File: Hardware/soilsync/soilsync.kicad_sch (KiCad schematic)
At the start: 3 parts, among them J1 Barrel_Jack_Switch, U1 STM32F103C8Tx, U2 LM2596

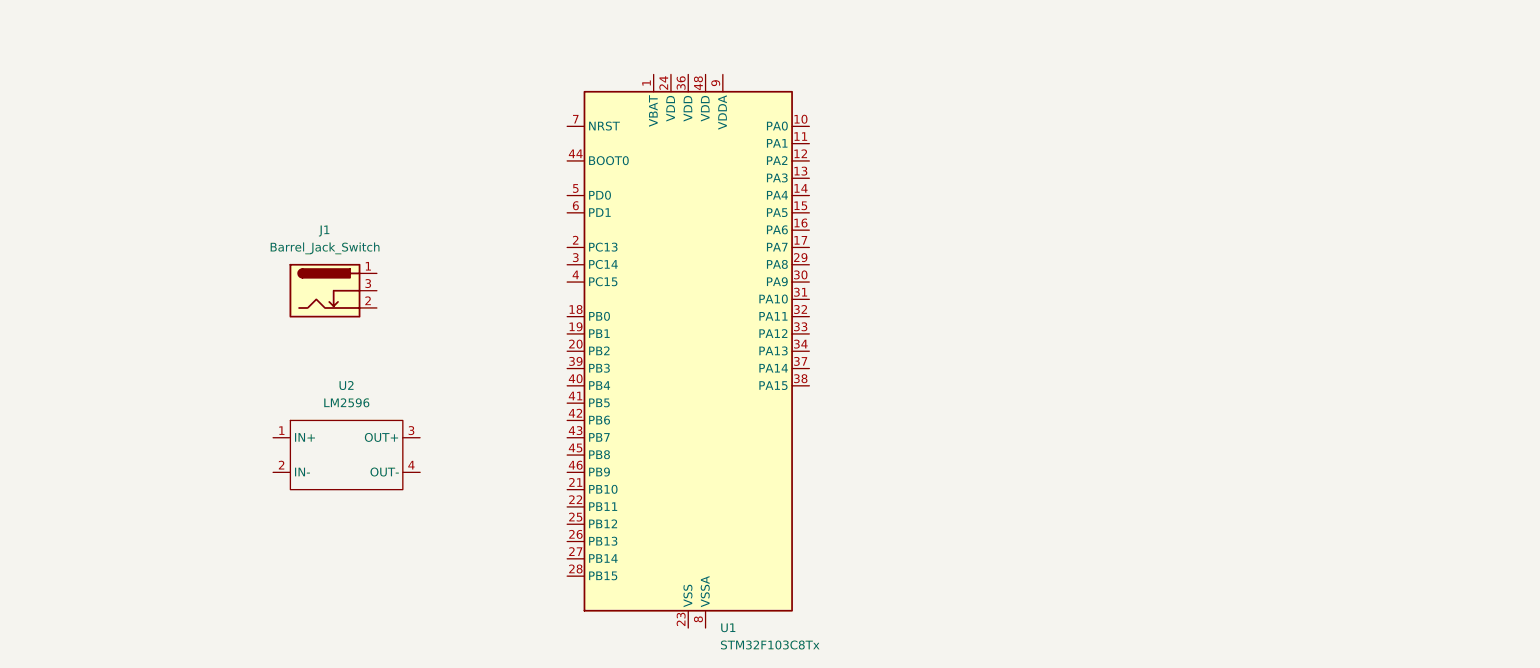
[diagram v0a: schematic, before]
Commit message: summary after classes
failed to create 3D model
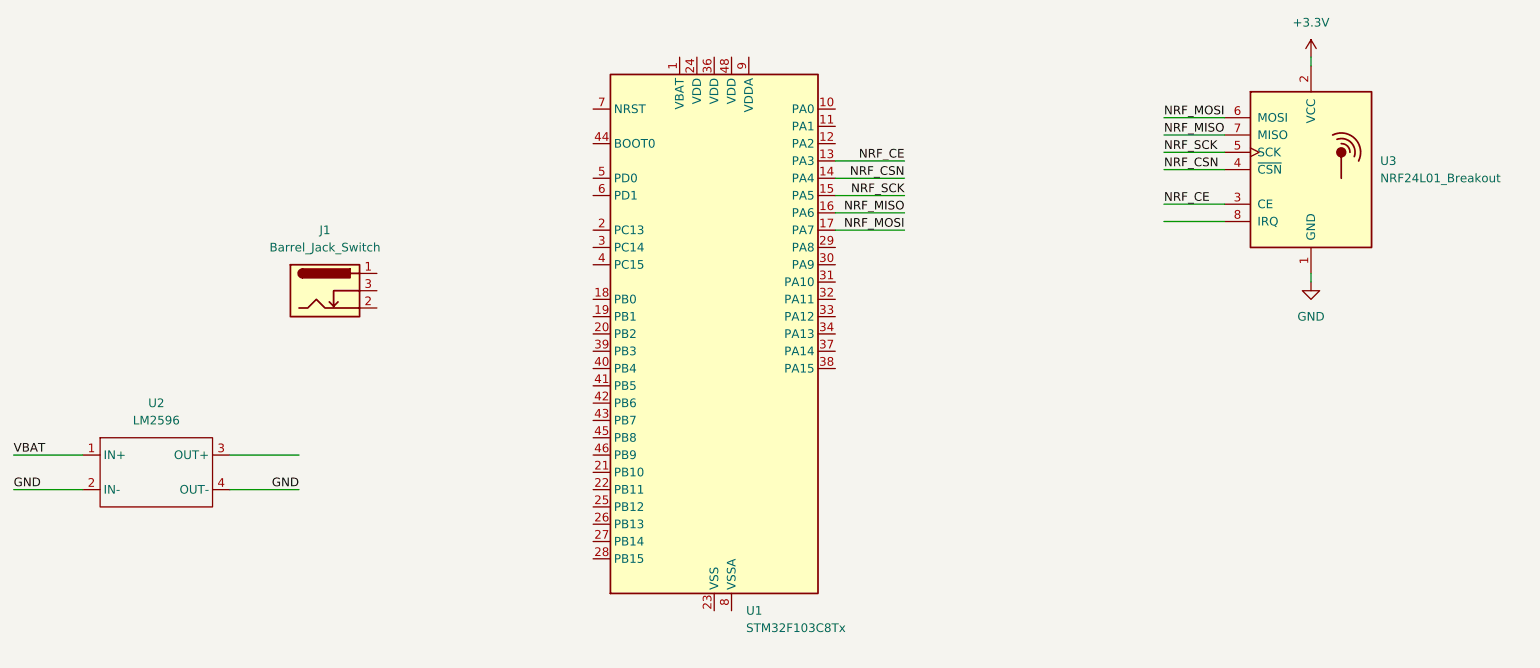
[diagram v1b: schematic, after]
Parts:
- added U3: NRF24L01_Breakout, RF_Module:nRF24L01_Breakout, symbol RF:NRF24L01_Breakout
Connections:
- net VBAT: now reaches U2.1 (IN+)
- net GND: now reaches U2.2 (IN-)
- net GND: now also U2.4 (OUT-), U3.1 (GND)
- net NRF_CE: now reaches U1.13 (PA3)
- net NRF_CE: now also U3.3 (CE)
- net NRF_CSN: now reaches U1.14 (PA4)
- net NRF_CSN: now also U3.4 (~{CSN})
- net NRF_SCK: now reaches U1.15 (PA5)
- net NRF_SCK: now also U3.5 (SCK)
- net NRF_MISO: now reaches U1.16 (PA6)
- net NRF_MISO: now also U3.7 (MISO)
- net NRF_MOSI: now reaches U1.17 (PA7)
- net NRF_MOSI: now also U3.6 (MOSI)
- new net +3.3V: U3.2 (VCC)
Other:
- moved on the sheet: U1, U2

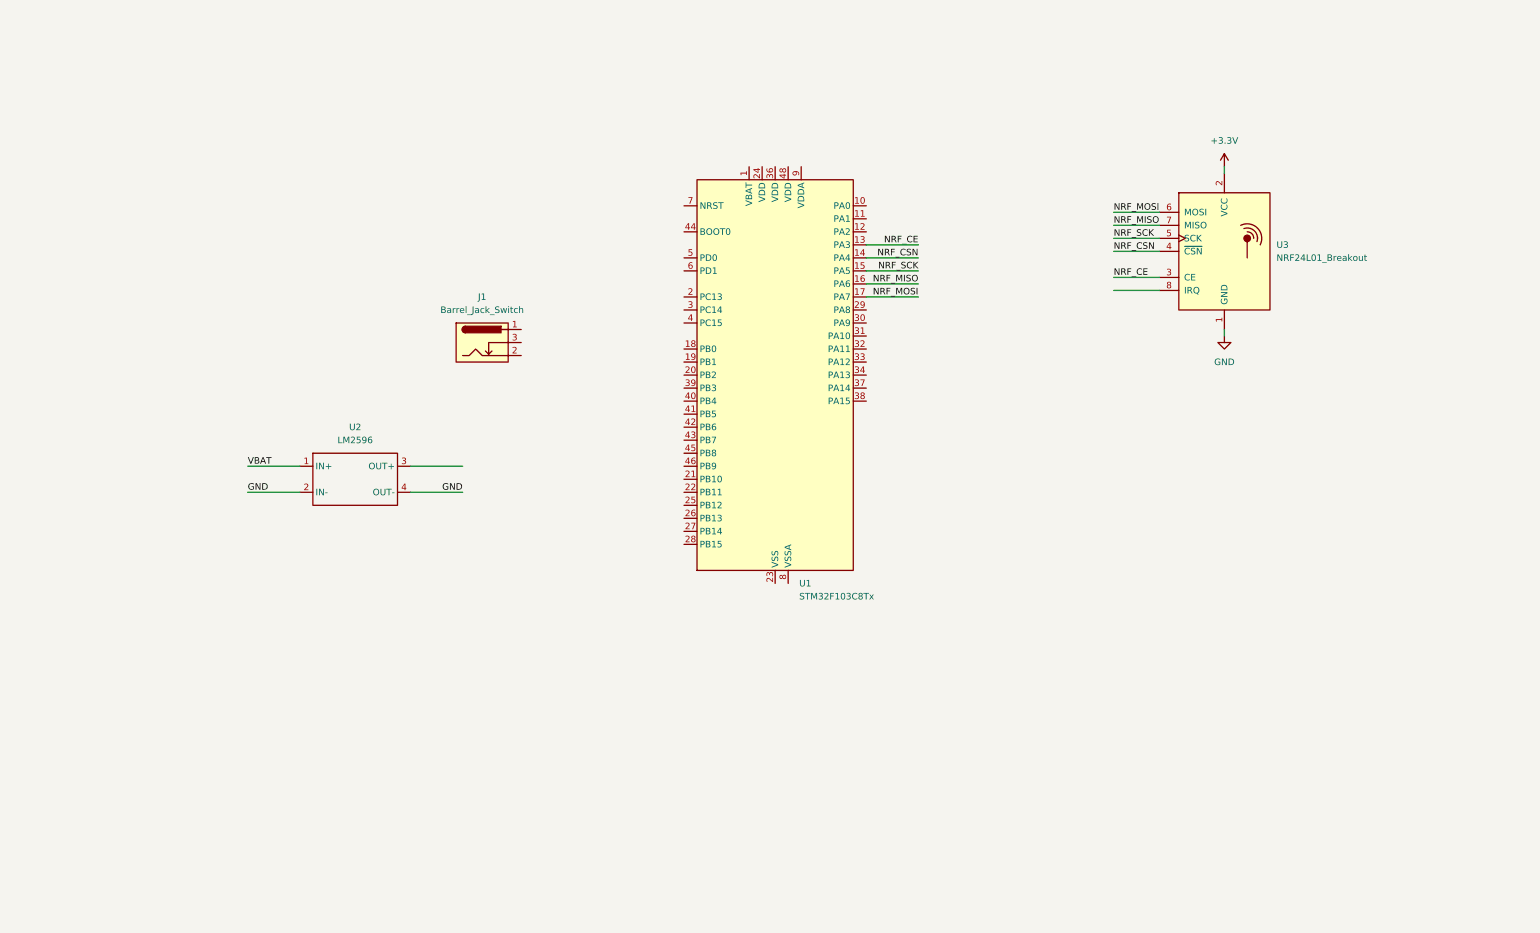
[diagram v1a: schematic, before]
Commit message: updated in kicad
added custom components
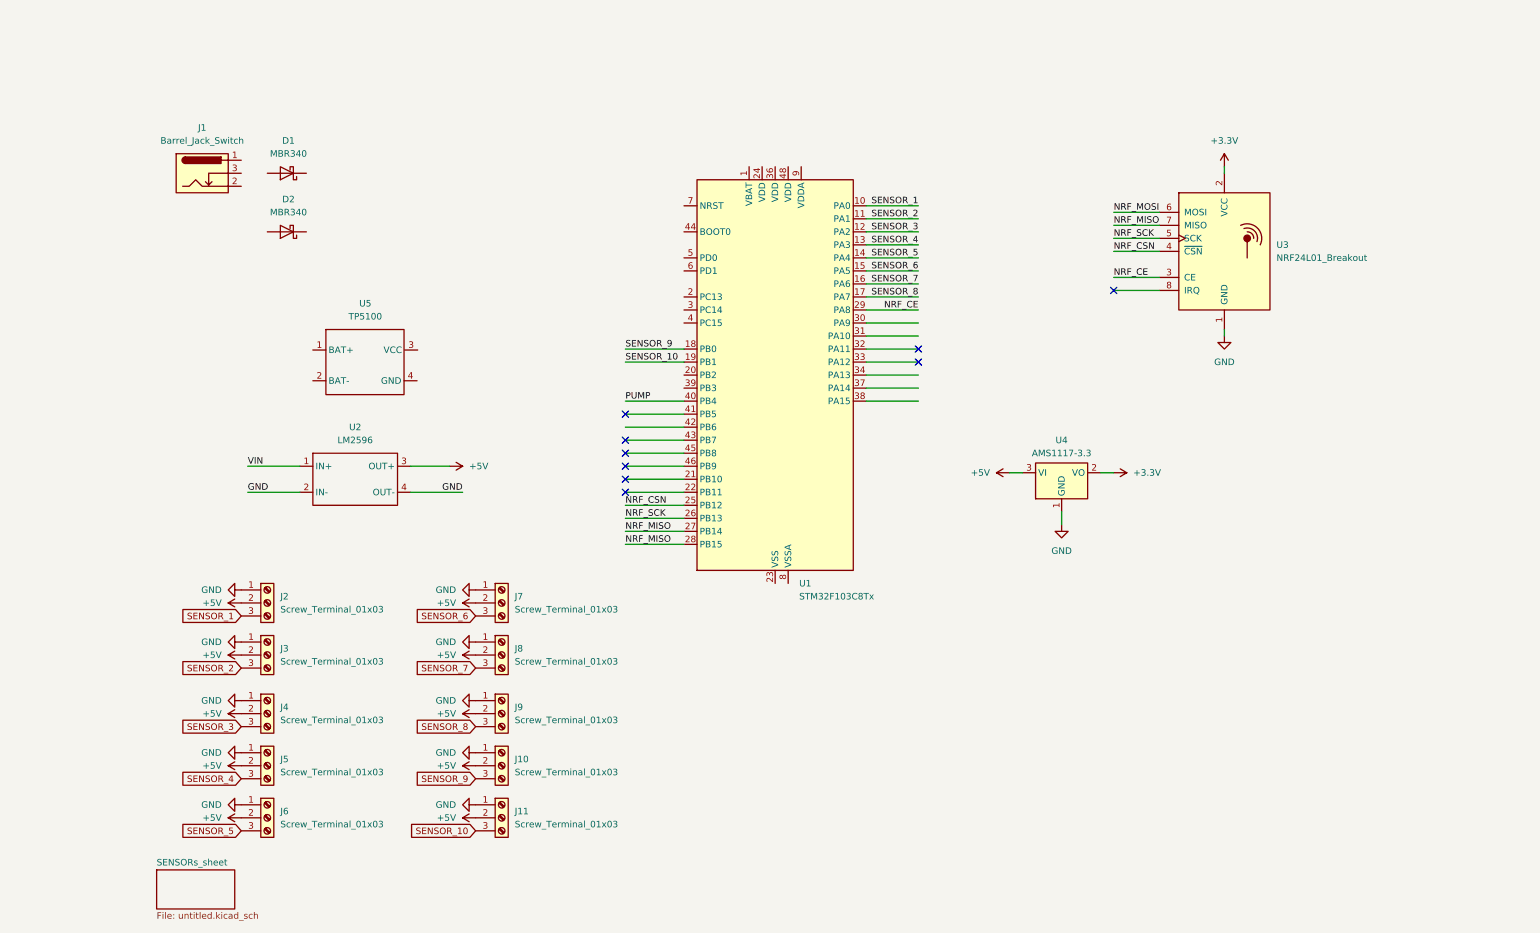
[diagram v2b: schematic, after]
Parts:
- added D1, D2: MBR340, Diode_THT:D_DO-201AD_P15.24mm_Horizontal, symbol Diode:MBR340
- added J10, J11, J2, J3, J4, J5, J6, J7, J8, J9: Screw_Terminal_01x03, TerminalBlock_4Ucon:TerminalBlock_4Ucon_1x03_P3.50mm_Horizontal, symbol Connector:Screw_Terminal_01x03
- added U4: AMS1117-3.3, Package_TO_SOT_SMD:SOT-223-3_TabPin2, symbol Regulator_Linear:AMS1117-3.3
- added U5: TP5100, Modules:TP5100_Module, symbol TP5100:TP5100_Module
- J1: footprint (none) -> Connector_BarrelJack:BarrelJack_Horizontal
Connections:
- net +3.3V: now also U4.2 (VO)
- net GND: now also J10.1 (Pin_1), J11.1 (Pin_1), J2.1 (Pin_1), J3.1 (Pin_1), J4.1 (Pin_1), J5.1 (Pin_1), J6.1 (Pin_1), J7.1 (Pin_1), J8.1 (Pin_1), J9.1 (Pin_1), U4.1 (GND)
- net NRF_CE: now also U1.29 (PA8); no longer U1.13 (PA3)
- net NRF_CSN: now also U1.25 (PB12); no longer U1.14 (PA4)
- net NRF_MISO: now also U1.27 (PB14), U1.28 (PB15); no longer U1.16 (PA6)
- net NRF_MOSI: no longer U1.17 (PA7)
- net NRF_SCK: now also U1.26 (PB13); no longer U1.15 (PA5)
- net +5V: now reaches U2.3 (OUT+)
- net +5V: now also J10.2 (Pin_2), J11.2 (Pin_2), J2.2 (Pin_2), J3.2 (Pin_2), J4.2 (Pin_2), J5.2 (Pin_2), J6.2 (Pin_2), J7.2 (Pin_2), J8.2 (Pin_2), J9.2 (Pin_2), U4.3 (VI)
- net SENSOR_1: now reaches U1.10 (PA0)
- net SENSOR_1: now also J2.3 (Pin_3)
- net SENSOR_2: now reaches U1.11 (PA1)
- net SENSOR_2: now also J3.3 (Pin_3)
- net SENSOR_3: now reaches U1.12 (PA2)
- net SENSOR_3: now also J4.3 (Pin_3)
- net SENSOR_9: now reaches U1.18 (PB0)
- net SENSOR_9: now also J10.3 (Pin_3)
- net SENSOR_10: now reaches U1.19 (PB1)
- net SENSOR_10: now also J11.3 (Pin_3)
- net PUMP: now reaches U1.40 (PB4)
- net VBAT renamed VIN
- new net SENSOR_4: J5.3 (Pin_3), U1.13 (PA3)
- new net SENSOR_5: J6.3 (Pin_3), U1.14 (PA4)
- new net SENSOR_6: J7.3 (Pin_3), U1.15 (PA5)
- new net SENSOR_7: J8.3 (Pin_3), U1.16 (PA6)
- new net SENSOR_8: J9.3 (Pin_3), U1.17 (PA7)
- no-connect marks 0 -> 9
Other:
- added sheet SENSORs_sheet (untitled.kicad_sch)
- moved on the sheet: J1

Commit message: a little changes in footprints
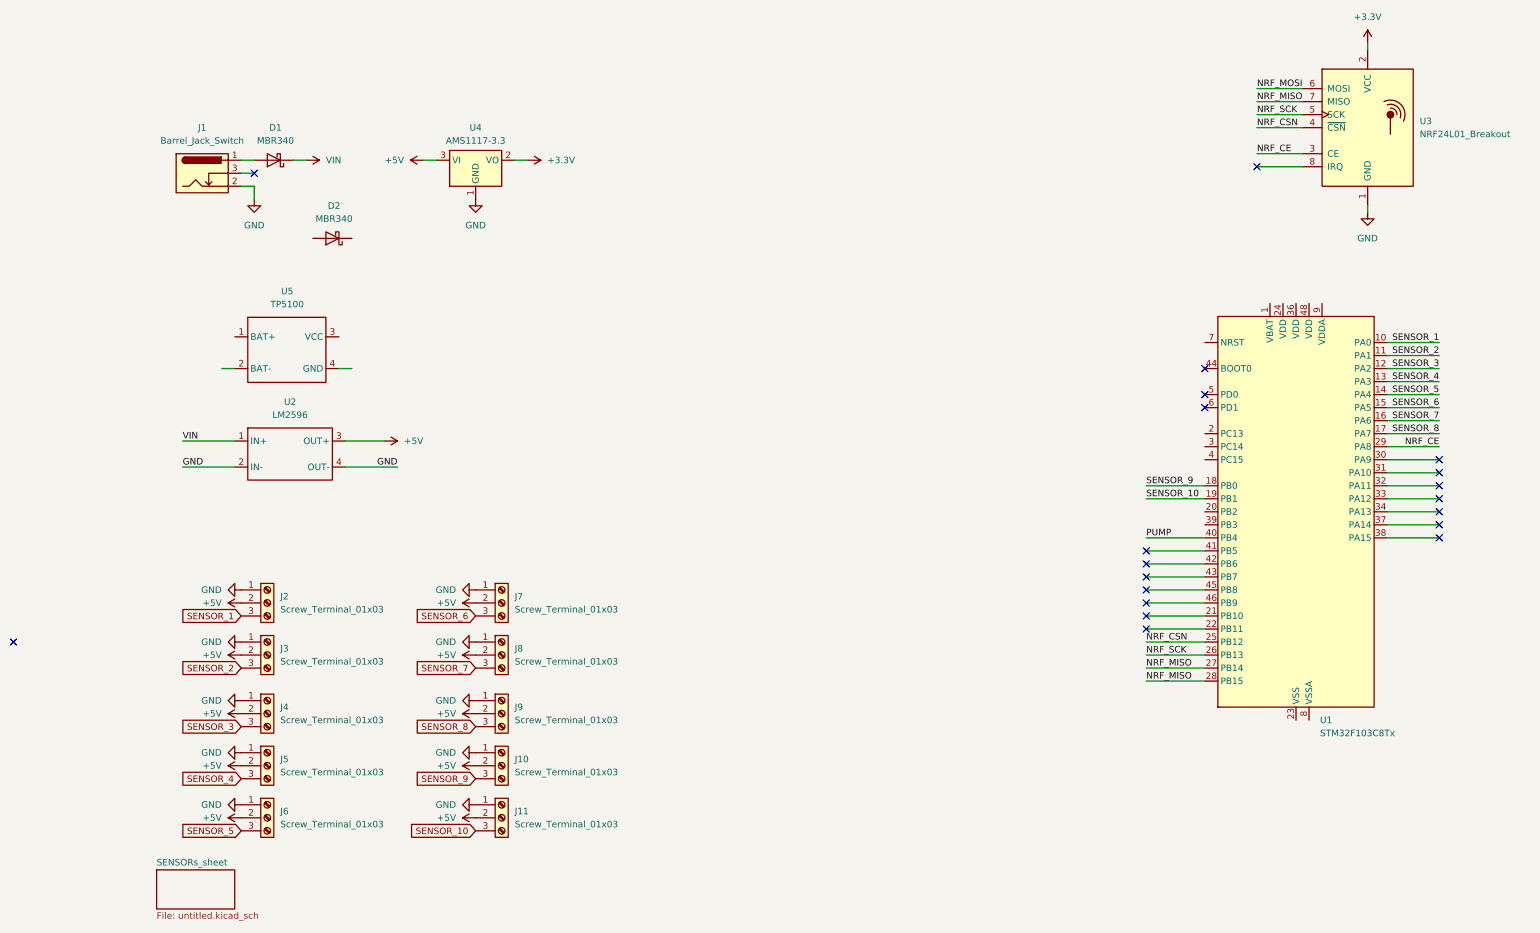
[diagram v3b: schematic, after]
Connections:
- net GND: now also J1.2
- net VIN: now also D1.1 (K)
- net at D1.2 (A): now also J1.1
- no-connect marks 9 -> 20
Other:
- moved on the sheet: D1, D2, U1, U2, U3, U4, U5

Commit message: custom components adjustments
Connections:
- net GND: now also U5.4 (GND)
- net VIN: now also U5.3 (VCC)
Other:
- removed sheet SENSORs_sheet
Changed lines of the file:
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@@
 	(wire
 		(pts
-			(xy 52.07 87.63) (xy 54.61 87.63)
+			(xy 52.07 87.63) (xy 57.15 87.63)
 		)
 		(stroke
@@
 	(wire
 		(pts
+			(xy 29.21 82.55) (xy 31.75 82.55)
+		)
+		(stroke
+			(width 0)
+			(type default)
+		)
+	)
+	(wire
+		(pts
 			(xy 53.34 101.76) (xy 60.96 101.76)
 		)
@@
 	(wire
 		(pts
+			(xy 57.15 87.63) (xy 57.15 88.9)
+		)
+		(stroke
+			(width 0)
+			(type default)
+		)
+	)
+	(wire
+		(pts
 			(xy 68.58 46.99) (xy 71.12 46.99)
 		)
@@
 	(wire
 		(pts
+			(xy 52.07 82.55) (xy 57.15 82.55)
+		)
+		(stroke
+			(width 0)
+			(type default)
+		)
+	)
+	(wire
+		(pts
 			(xy 33.02 46.99) (xy 35.56 46.99)
 		)
@@
 		)
 	)
+	(label "VIN"
+		(at 57.15 82.55 180)
+		(effects
+			(font
+				(size 1.27 1.27)
+			)
+			(justify right bottom)
+		)
+	)
 	(label "SENSOR_1"
 		(at 266.7 82.55 180)
@@
 	)
 	(symbol
-		(lib_id "power:+5V")
-		(at 78.74 154.94 90)
+		(lib_id "power:GND")
+		(at 57.15 88.9 0)
 		(unit 1)
 		(exclude_from_sim no)
@@
 		(dnp no)
 		(fields_autoplaced yes)
-		(property "Reference" "#PWR014"
-			(at 82.55 154.94 0)
+		(property "Reference" "#PWR029"
+			(at 57.15 95.25 0)
 			(effects
 				(font
@@
 			)
 		)
-		(property "Value" "+5V"
-			(at 74.93 154.9399 90)
+		(property "Value" "GND"
+			(at 57.15 93.98 0)
 			(effects
 				(font
 					(size 1.27 1.27)
 				)
-				(justify left)
 			)
 		)
 		(property "Footprint" ""
-			(at 78.74 154.94 0)
+			(at 57.15 88.9 0)
 			(effects
 				(font
@@
 		)
 		(property "Datasheet" ""
-			(at 78.74 154.94 0)
+			(at 57.15 88.9 0)
 			(effects
 				(font
@@
 			)
 		)
-		(property "Description" "Power symbol creates a global label with name \"+5V\""
-			(at 78.74 154.94 0)
+		(property "Description" "Power symbol creates a global label with name \"GND\" , ground"
+			(at 57.15 88.9 0)
 			(effects
 				(font
@@
 			(project ""
 				(path "/3e3c5228-e247-4567-a085-5b3516ef26ec"
-					(reference "#PWR014")
+					(reference "#PWR029")
 					(unit 1)
 				)
@@
 		)
 	)
-	(sheet
-		(at 16.51 185.42)
-		(size 15.24 7.62)
+	(symbol
+		(lib_id "power:+5V")
+		(at 78.74 154.94 90)
+		(unit 1)
 		(exclude_from_sim no)
 		(in_bom yes)
@@
 		(dnp no)
 		(fields_autoplaced yes)
-		(stroke
-			(width 0.1524)
-			(type solid)
+		(property "Reference" "#PWR014"
+			(at 82.55 154.94 0)
+			(effects
+				(font
+					(size 1.27 1.27)
+				)
+				(hide yes)
+			)
+		)
+		(property "Value" "+5V"
+			(at 74.93 154.9399 90)
+			(effects
+				(font
+					(size 1.27 1.27)
+				)
+				(justify left)
+			)
 		)
-		(fill
-			(color 0 0 0 0.0000)
+		(property "Footprint" ""
+			(at 78.74 154.94 0)
+			(effects
+				(font
+					(size 1.27 1.27)
+				)
+				(hide yes)
+			)
 		)
-		(property "Sheetname" "SENSORs_sheet"
-			(at 16.51 184.7084 0)
+		(property "Datasheet" ""
+			(at 78.74 154.94 0)
 			(effects
 				(font
 					(size 1.27 1.27)
 				)
-				(justify left bottom)
+				(hide yes)
 			)
 		)
-		(property "Sheetfile" "untitled.kicad_sch"
-			(at 16.51 193.6246 0)
+		(property "Description" "Power symbol creates a global label with name \"+5V\""
+			(at 78.74 154.94 0)
 			(effects
 				(font
 					(size 1.27 1.27)
 				)
-				(justify left top)
+				(hide yes)
 			)
 		)
+		(pin "1"
+		)
 		(instances
-			(project "soilsync"
+			(project ""
 				(path "/3e3c5228-e247-4567-a085-5b3516ef26ec"
-					(page "2")
+					(reference "#PWR014")
+					(unit 1)
 				)
 			)

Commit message: major PCB updates
placement & routing
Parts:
- added J12: Screw_Terminal_01x03, TerminalBlock_4Ucon:TerminalBlock_4Ucon_1x03_P3.50mm_Horizontal, symbol Connector:Screw_Terminal_01x03
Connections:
- net +5V: now also U1.23 (VSS), U1.35 (VSS), U1.47 (VSS), J12.2 (Pin_2)
- net GND: now also J12.1 (Pin_1)
- net PUMP: now also J12.3 (Pin_3)
- net VIN: now also D2.1 (K); no longer U5.3 (VCC)
- net at D2.2 (A): now also U5.3 (VCC)
- net BAT+: now reaches U5.1 (BAT+)
- net BAT-: now reaches U5.2 (BAT-)
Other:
- moved on the sheet: D2

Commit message: Layout adjustments
tbf
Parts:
- added J13: Screw_Terminal_01x02, symbol Connector:Screw_Terminal_01x02
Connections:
- net GND: now also J13.2 (Pin_2)
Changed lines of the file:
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@@
+	)
+	(symbol
+		(lib_id "power:GND")
+		(at 33.02 123.19 270)
+		(unit 1)
+		(exclude_from_sim no)
+		(in_bom yes)
+		(on_board yes)
+		(dnp no)
+		(fields_autoplaced yes)
+		(property "Reference" "#PWR033"
+			(at 26.67 123.19 0)
+			(effects
+				(font
+					(size 1.27 1.27)
+				)
+				(hide yes)
+			)
+		)
+		(property "Value" "GND"
+			(at 29.21 123.1899 90)
+			(effects
+				(font
+					(size 1.27 1.27)
+				)
+				(justify right)
+			)
+		)
+		(property "Footprint" ""
+			(at 33.02 123.19 0)
+			(effects
+				(font
+					(size 1.27 1.27)
+				)
+				(hide yes)
+			)
+		)
+		(property "Datasheet" ""
+			(at 33.02 123.19 0)
+			(effects
+				(font
+					(size 1.27 1.27)
+				)
+				(hide yes)
+			)
+		)
+		(property "Description" "Power symbol creates a global label with name \"GND\" , ground"
+			(at 33.02 123.19 0)
+			(effects
+				(font
+					(size 1.27 1.27)
+				)
+				(hide yes)
+			)
+		)
+		(pin "1"
+		)
+		(instances
+			(project ""
+				(path "/3e3c5228-e247-4567-a085-5b3516ef26ec"
+					(reference "#PWR033")
+					(unit 1)
+				)
+			)
+		)
 	)
 	(symbol
@@
 					(unit 1)
 				)
+			)
+		)
+	)
+	(symbol
+		(lib_id "Connector:Screw_Terminal_01x02")
+		(at 38.1 120.65 0)
+		(unit 1)
+		(exclude_from_sim no)
+		(in_bom yes)
+		(on_board yes)
+		(dnp no)
+		(fields_autoplaced yes)
+		(property "Reference" "J13"
+			(at 40.64 120.6499 0)
+			(effects
+				(font
+					(size 1.27 1.27)
+				)
+				(justify left)
+			)
+		)
+		(property "Value" "Screw_Terminal_01x02"
+			(at 40.64 123.1899 0)
+			(effects
+				(font
+					(size 1.27 1.27)
+				)
+				(justify left)
+			)
+		)
+		(property "Footprint" ""
+			(at 38.1 120.65 0)
+			(effects
+				(font
+					(size 1.27 1.27)
+				)
+				(hide yes)
+			)
+		)
+		(property "Datasheet" "~"
+			(at 38.1 120.65 0)
+			(effects
+				(font
+					(size 1.27 1.27)
+				)
+				(hide yes)
+			)
+		)
+		(property "Description" "Generic screw terminal, single row, 01x02, script generated (kicad-library-utils/schlib/autogen/connector/)"
+			(at 38.1 120.65 0)
+			(effects
+				(font
+					(size 1.27 1.27)
+				)
+				(hide yes)
+			)
+		)
+		(pin "1"
+		)
+		(pin "2"
+		)
+		(instances
+			(project ""
+				(path "/3e3c5228-e247-4567-a085-5b3516ef26ec"
+					(reference "J13")
+					(unit 1)
+				)
